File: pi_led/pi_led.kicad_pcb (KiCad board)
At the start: 2 copper layers, 50 x 50 mm, 13 parts, among them CON1 PWR, P1 LED_STRIP, P2 RiPi, Q1 STP16NF06L, Q2 STP16NF06L, Q3 STP16NF06L

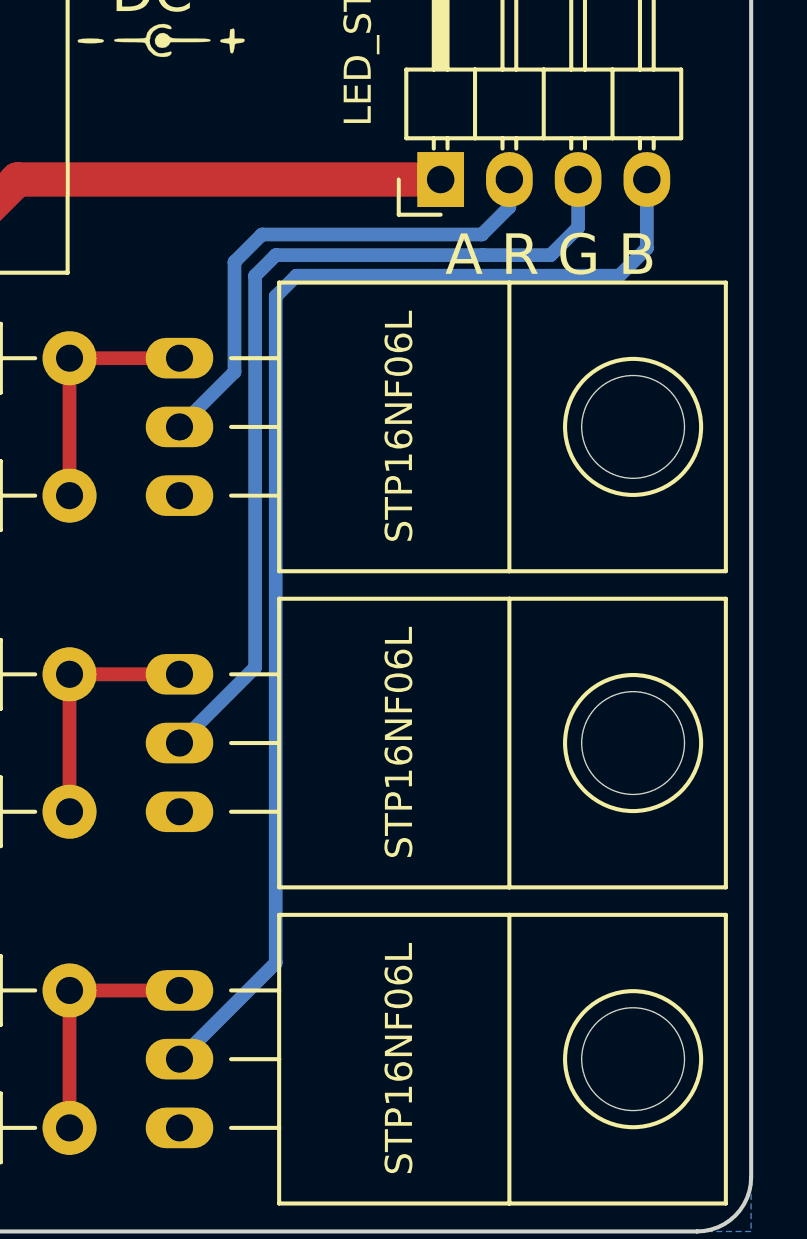
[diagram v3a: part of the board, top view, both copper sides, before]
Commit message: Change LED->MOSFET tracks back to 50mil
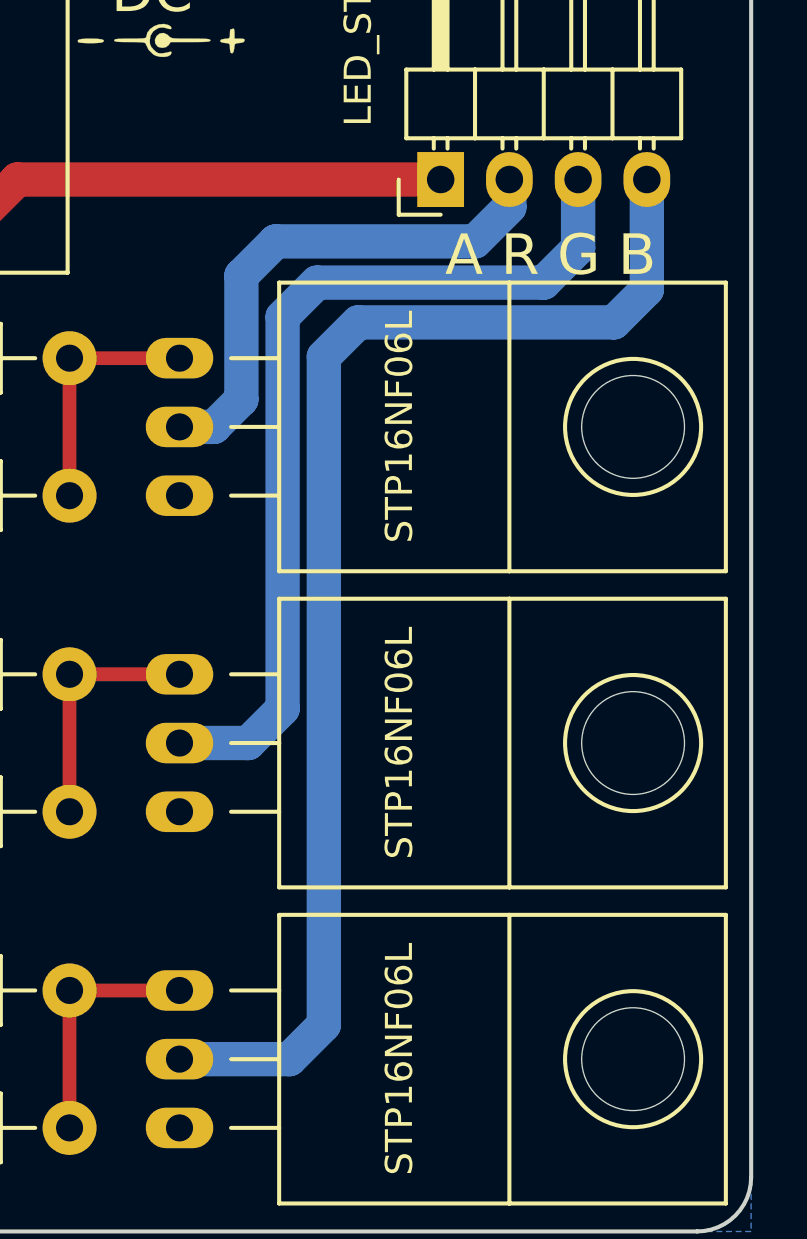
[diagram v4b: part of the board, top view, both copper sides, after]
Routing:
- net /LED_B: track 46.7 -> 47.6 mm
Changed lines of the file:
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@@
     (thickness 1.6)
     (drawings 11)
-    (tracks 41)
+    (tracks 42)
     (zones 0)
     (modules 13)
@@
   )
   (setup
-    (last_trace_width 0.508)
+    (last_trace_width 1.27)
     (user_trace_width 0.254)
     (user_trace_width 0.508)
@@
   (segment (start 110.236 73.76414) (end 112.88014 71.12) (width 1.27) (layer F.Cu) (net 1) (status 400000))
   (segment (start 112.88014 71.12) (end 128.524 71.12) (width 1.27) (layer F.Cu) (net 1) (status 800000))
-  (segment (start 130.048 73.152) (end 121.92 73.152) (width 0.508) (layer B.Cu) (net 3))
-  (segment (start 131.064 72.136) (end 130.048 73.152) (width 0.508) (layer B.Cu) (net 3) (status 400000))
-  (segment (start 120.904 78.232) (end 118.872 80.264) (width 0.508) (layer B.Cu) (net 3) (status 800000))
-  (segment (start 120.904 74.168) (end 120.904 78.232) (width 0.508) (layer B.Cu) (net 3))
-  (segment (start 121.92 73.152) (end 120.904 74.168) (width 0.508) (layer B.Cu) (net 3))
-  (segment (start 131.064 71.12) (end 131.064 72.136) (width 0.508) (layer B.Cu) (net 3) (status C00000))
-  (segment (start 130.101998 73.914) (end 122.428 73.914) (width 0.508) (layer B.Cu) (net 4))
-  (segment (start 133.604 71.12) (end 133.604 72.898) (width 0.508) (layer B.Cu) (net 4) (status 400000))
-  (segment (start 133.604 72.898) (end 132.588 73.914) (width 0.508) (layer B.Cu) (net 4))
-  (segment (start 132.588 73.914) (end 130.101998 73.914) (width 0.508) (layer B.Cu) (net 4))
-  (segment (start 121.666 89.154) (end 118.872 91.948) (width 0.508) (layer B.Cu) (net 4) (status 800000))
-  (segment (start 121.666 74.676) (end 121.666 89.154) (width 0.508) (layer B.Cu) (net 4))
-  (segment (start 122.428 73.914) (end 121.666 74.676) (width 0.508) (layer B.Cu) (net 4))
-  (segment (start 130.048 74.676) (end 123.19 74.676) (width 0.508) (layer B.Cu) (net 5))
-  (segment (start 136.144 71.12) (end 136.144 73.66) (width 0.508) (layer B.Cu) (net 5) (status 400000))
-  (segment (start 136.144 73.66) (end 135.128 74.676) (width 0.508) (layer B.Cu) (net 5))
-  (segment (start 130.048 74.676) (end 135.128 74.676) (width 0.508) (layer B.Cu) (net 5))
-  (segment (start 122.428 100.076) (end 118.872 103.632) (width 0.508) (layer B.Cu) (net 5) (status 800000))
-  (segment (start 122.428 75.438) (end 122.428 100.076) (width 0.508) (layer B.Cu) (net 5))
-  (segment (start 123.19 74.676) (end 122.428 75.438) (width 0.508) (layer B.Cu) (net 5))
+  (segment (start 131.064 71.12) (end 131.064 72.136) (width 1.27) (layer B.Cu) (net 3) (status C00000))
+  (segment (start 131.064 72.136) (end 129.794 73.406) (width 1.27) (layer B.Cu) (net 3) (status 400000))
+  (segment (start 129.794 73.406) (end 122.428 73.406) (width 1.27) (layer B.Cu) (net 3))
+  (segment (start 122.428 73.406) (end 121.158 74.676) (width 1.27) (layer B.Cu) (net 3))
+  (segment (start 121.158 74.676) (end 121.158 79.248) (width 1.27) (layer B.Cu) (net 3))
+  (segment (start 121.158 79.248) (end 120.142 80.264) (width 1.27) (layer B.Cu) (net 3))
+  (segment (start 120.142 80.264) (end 118.872 80.264) (width 1.27) (layer B.Cu) (net 3) (status 800000))
+  (segment (start 133.604 71.12) (end 133.604 73.66) (width 1.27) (layer B.Cu) (net 4) (status 400000))
+  (segment (start 121.412 91.948) (end 118.872 91.948) (width 1.27) (layer B.Cu) (net 4) (status 800000))
+  (segment (start 122.682 90.678) (end 121.412 91.948) (width 1.27) (layer B.Cu) (net 4))
+  (segment (start 122.682 76.2) (end 122.682 90.678) (width 1.27) (layer B.Cu) (net 4))
+  (segment (start 123.952 74.93) (end 122.682 76.2) (width 1.27) (layer B.Cu) (net 4))
+  (segment (start 132.334 74.93) (end 123.952 74.93) (width 1.27) (layer B.Cu) (net 4))
+  (segment (start 133.604 73.66) (end 132.334 74.93) (width 1.27) (layer B.Cu) (net 4))
+  (segment (start 136.144 71.12) (end 136.144 75.184) (width 1.27) (layer B.Cu) (net 5) (status 400000))
+  (segment (start 122.936 103.632) (end 118.872 103.632) (width 1.27) (layer B.Cu) (net 5) (status 800000))
+  (segment (start 124.206 102.362) (end 122.936 103.632) (width 1.27) (layer B.Cu) (net 5))
+  (segment (start 124.206 77.670002) (end 124.206 102.362) (width 1.27) (layer B.Cu) (net 5))
+  (segment (start 125.476 76.400002) (end 124.206 77.670002) (width 1.27) (layer B.Cu) (net 5))
+  (segment (start 134.927998 76.400002) (end 125.476 76.400002) (width 1.27) (layer B.Cu) (net 5))
+  (segment (start 136.144 75.184) (end 134.927998 76.400002) (width 1.27) (layer B.Cu) (net 5))
   (segment (start 94.996 104.14) (end 98.044 101.092) (width 0.508) (layer F.Cu) (net 6) (status 400000))
   (segment (start 98.044 101.092) (end 104.648 101.092) (width 0.508) (layer F.Cu) (net 6) (status 800000))

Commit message: Add more GND, add board info
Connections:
- P2 pad 1: (no net) -> Net-(P2-Pad1)
- P2 pad 10: (no net) -> Net-(P2-Pad10)
- P2 pad 11: (no net) -> Net-(P2-Pad11)
- P2 pad 12: (no net) -> Net-(P2-Pad12)
- P2 pad 13: (no net) -> Net-(P2-Pad13)
- P2 pad 14: (no net) -> GND
- P2 pad 15: (no net) -> Net-(P2-Pad15)
- P2 pad 16: (no net) -> Net-(P2-Pad16)
- P2 pad 17: (no net) -> Net-(P2-Pad17)
- P2 pad 18: (no net) -> Net-(P2-Pad18)
- P2 pad 19: (no net) -> Net-(P2-Pad19)
- P2 pad 2: (no net) -> Net-(P2-Pad2)
- P2 pad 20: (no net) -> GND
- P2 pad 21: (no net) -> Net-(P2-Pad21)
- P2 pad 22: (no net) -> Net-(P2-Pad22)
- P2 pad 23: (no net) -> Net-(P2-Pad23)
- P2 pad 24: (no net) -> Net-(P2-Pad24)
- P2 pad 25: (no net) -> GND
- P2 pad 26: (no net) -> Net-(P2-Pad26)
- P2 pad 27: (no net) -> Net-(P2-Pad27)
- P2 pad 28: (no net) -> Net-(P2-Pad28)
- P2 pad 29: (no net) -> Net-(P2-Pad29)
- P2 pad 30: (no net) -> GND
- P2 pad 31: (no net) -> Net-(P2-Pad31)
- P2 pad 32: (no net) -> Net-(P2-Pad32)
- P2 pad 33: (no net) -> Net-(P2-Pad33)
- P2 pad 34: (no net) -> GND
- P2 pad 35: (no net) -> Net-(P2-Pad35)
- P2 pad 36: (no net) -> Net-(P2-Pad36)
- P2 pad 4: (no net) -> Net-(P2-Pad4)
- P2 pad 6: (no net) -> GND
- P2 pad 8: (no net) -> Net-(P2-Pad8)
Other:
- board text added: "Pi-LED v0.1 15/08/15 Hark <boards@harkonen.net>"

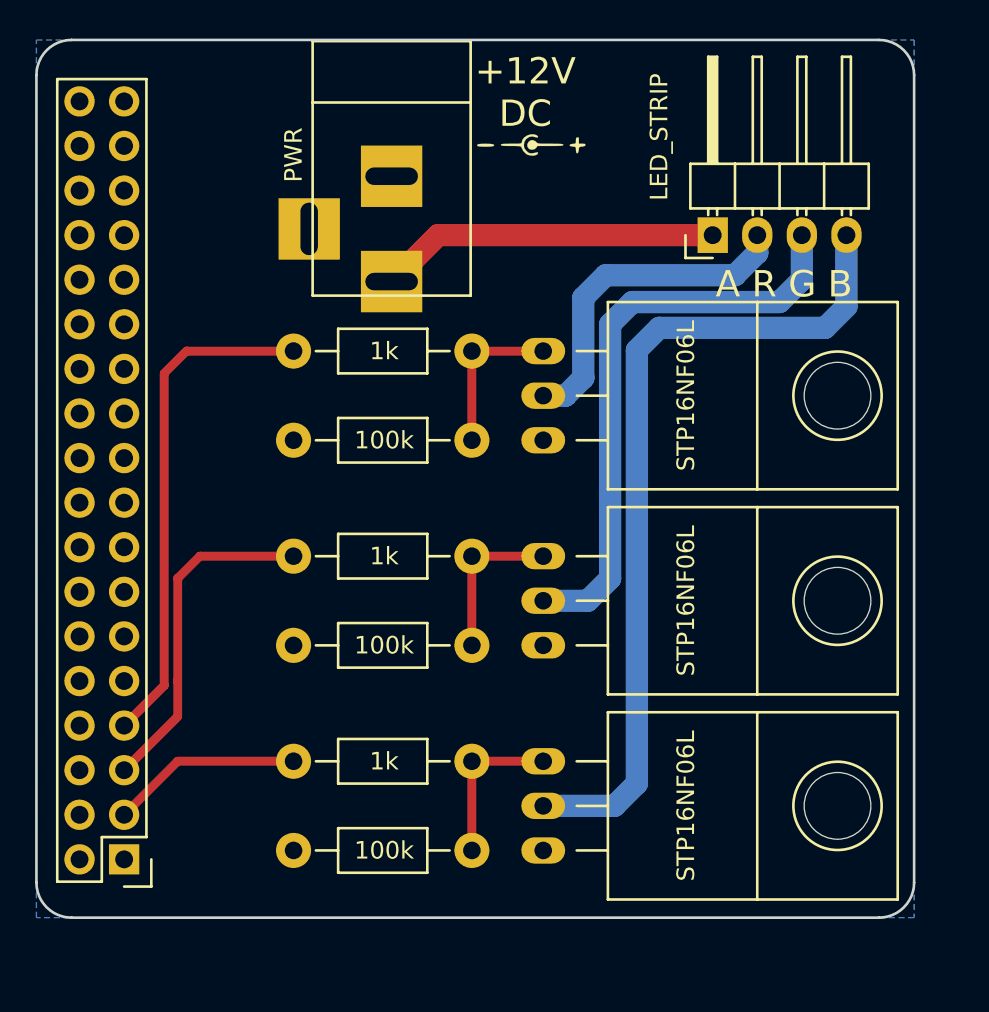
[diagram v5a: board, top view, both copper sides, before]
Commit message: Added front ground net
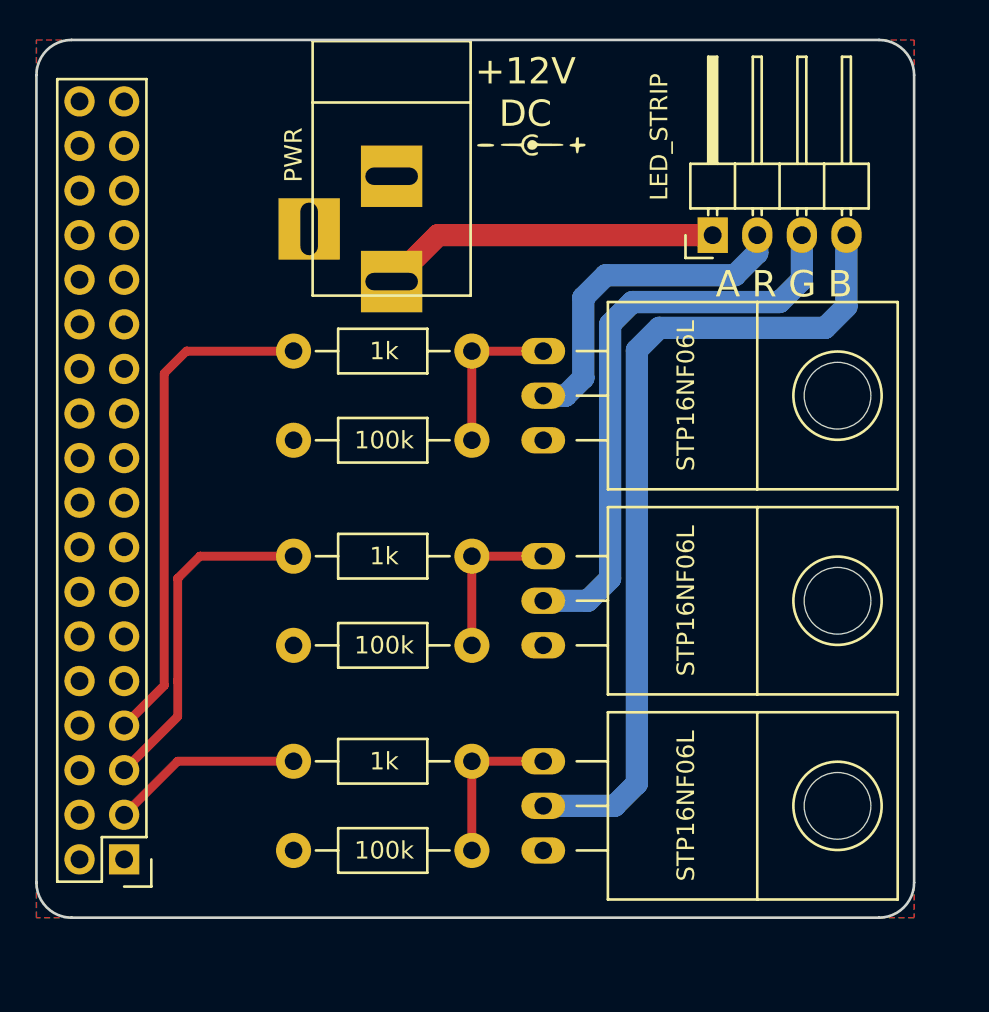
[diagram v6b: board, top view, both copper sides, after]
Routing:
- added copper zone on F.Cu, net GND
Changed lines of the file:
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@@
   (layers
     (0 F.Cu signal)
-    (31 B.Cu signal hide)
+    (31 B.Cu signal)
     (32 B.Adhes user)
     (33 F.Adhes user)
@@
     (user_trace_width 1.27)
     (trace_clearance 0.2)
-    (zone_clearance 0.381)
+    (zone_clearance 0.508)
     (zone_45_only no)
     (trace_min 0.2032)
@@
       )
     )
+  )
+  (zone (net 2) (net_name GND) (layer F.Cu) (hatch edge 0.508)
+    (connect_pads (clearance 0.508))
+    (min_thickness 0.254)
+    (fill yes (arc_segments 16) (thermal_gap 0.508) (thermal_bridge_width 0.508))
+    (polygon
+      (pts
+        (xy 140 110) (xy 90 110) (xy 90 60) (xy 140 60) (xy 140 110)
+      )
+    )
+  )
+  (zone (net 0) (net_name "") (layer F.Cu) (hatch edge 0.508)
+    (connect_pads (clearance 0.508))
+    (min_thickness 0.254)
+    (keepout (tracks not_allowed) (vias not_allowed) (copperpour not_allowed))
+    (fill (arc_segments 16) (thermal_gap 0.508) (thermal_bridge_width 0.508))
+    (polygon
+      (pts
+        (xy 139.192 109.22) (xy 122.428 109.22) (xy 122.428 74.676) (xy 139.192 74.676) (xy 139.192 109.22)
+      )
+    )

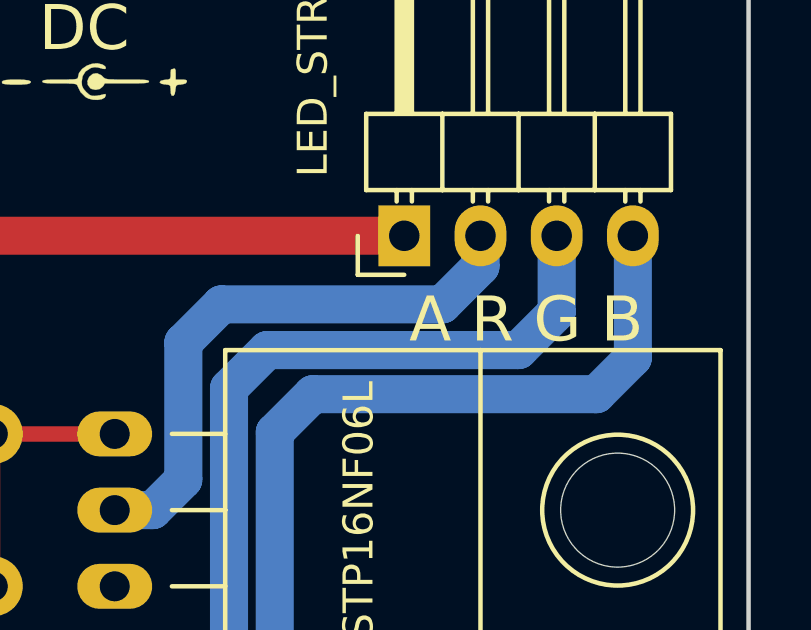
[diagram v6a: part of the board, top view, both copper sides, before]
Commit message: Back keepout for MOSFET washers
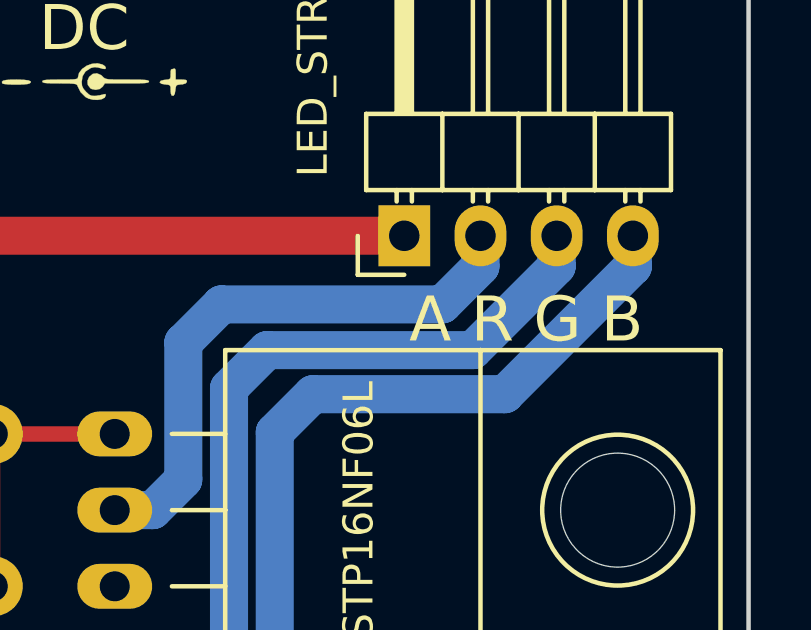
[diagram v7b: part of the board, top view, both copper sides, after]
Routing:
- net /LED_B: track 47.6 -> 45.8 mm
- net /LED_G: track 33.3 -> 32.4 mm
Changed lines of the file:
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@@
     (trace_clearance 0.2)
     (zone_clearance 0.508)
-    (zone_45_only no)
+    (zone_45_only yes)
     (trace_min 0.2032)
     (segment_width 0.2)
@@
   (segment (start 121.158 79.248) (end 120.142 80.264) (width 1.27) (layer B.Cu) (net 3))
   (segment (start 120.142 80.264) (end 118.872 80.264) (width 1.27) (layer B.Cu) (net 3))
-  (segment (start 133.604 71.12) (end 133.604 73.66) (width 1.27) (layer B.Cu) (net 4))
+  (segment (start 133.604 71.12) (end 133.604 72.136) (width 1.27) (layer B.Cu) (net 4))
   (segment (start 121.412 91.948) (end 118.872 91.948) (width 1.27) (layer B.Cu) (net 4))
   (segment (start 122.682 90.678) (end 121.412 91.948) (width 1.27) (layer B.Cu) (net 4))
   (segment (start 122.682 76.2) (end 122.682 90.678) (width 1.27) (layer B.Cu) (net 4))
   (segment (start 123.952 74.93) (end 122.682 76.2) (width 1.27) (layer B.Cu) (net 4))
-  (segment (start 132.334 74.93) (end 123.952 74.93) (width 1.27) (layer B.Cu) (net 4))
-  (segment (start 133.604 73.66) (end 132.334 74.93) (width 1.27) (layer B.Cu) (net 4))
-  (segment (start 136.144 71.12) (end 136.144 75.184) (width 1.27) (layer B.Cu) (net 5))
+  (segment (start 130.81 74.93) (end 123.952 74.93) (width 1.27) (layer B.Cu) (net 4))
+  (segment (start 133.604 72.136) (end 130.81 74.93) (width 1.27) (layer B.Cu) (net 4))
+  (segment (start 136.144 71.12) (end 136.144 72.136) (width 1.27) (layer B.Cu) (net 5))
   (segment (start 122.936 103.632) (end 118.872 103.632) (width 1.27) (layer B.Cu) (net 5))
   (segment (start 124.206 102.362) (end 122.936 103.632) (width 1.27) (layer B.Cu) (net 5))
   (segment (start 124.206 77.670002) (end 124.206 102.362) (width 1.27) (layer B.Cu) (net 5))
   (segment (start 125.476 76.400002) (end 124.206 77.670002) (width 1.27) (layer B.Cu) (net 5))
-  (segment (start 134.927998 76.400002) (end 125.476 76.400002) (width 1.27) (layer B.Cu) (net 5))
-  (segment (start 136.144 75.184) (end 134.927998 76.400002) (width 1.27) (layer B.Cu) (net 5))
+  (segment (start 131.879998 76.400002) (end 125.476 76.400002) (width 1.27) (layer B.Cu) (net 5))
+  (segment (start 136.144 72.136) (end 131.879998 76.400002) (width 1.27) (layer B.Cu) (net 5))
   (segment (start 94.996 104.14) (end 98.044 101.092) (width 0.508) (layer F.Cu) (net 6))
   (segment (start 98.044 101.092) (end 104.648 101.092) (width 0.508) (layer F.Cu) (net 6))
@@
       )
     )
+  )
+  (zone (net 0) (net_name "") (layer B.Cu) (hatch edge 0.508)
+    (connect_pads (clearance 0.508))
+    (min_thickness 0.254)
+    (keepout (tracks not_allowed) (vias not_allowed) (copperpour not_allowed))
+    (fill (arc_segments 16) (thermal_gap 0.508) (thermal_bridge_width 0.508))
+    (polygon
+      (pts
+        (xy 139.5 109.5) (xy 130.5 109.5) (xy 131 77.5) (xy 131.5 77.5) (xy 132.5 77)
+        (xy 134 75.5) (xy 139.5 75.5)
+      )
+    )
